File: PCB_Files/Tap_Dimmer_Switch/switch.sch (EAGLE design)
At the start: 37 parts, among them P1 HT7333

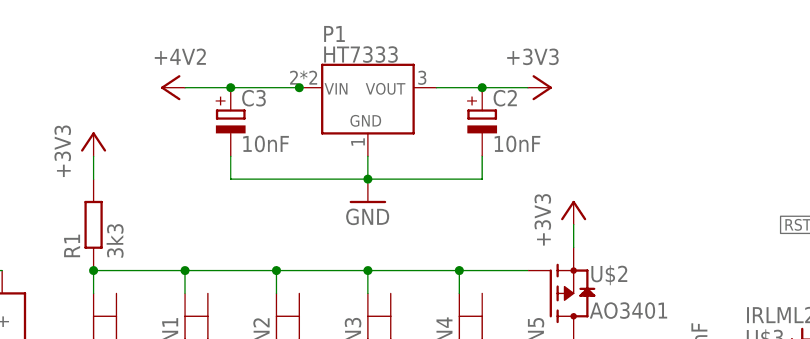
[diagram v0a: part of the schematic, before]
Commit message: created additional compact design of ws2812b module
this new design features smaller footprint, but the esp module ist partially outside the board, which will result in better wifi connection.

additionally the footprint of the HT7333 has been fixed as previously it had used the wrong package.
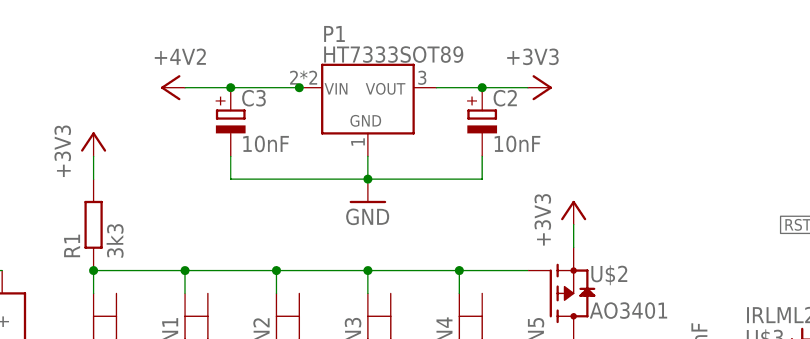
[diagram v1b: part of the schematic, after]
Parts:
- P1: value HT7333 -> HT7333SOT89; device diyHue:HT7333 -> diyHue:HT7333SOT89
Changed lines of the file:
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@@
 <part name="C1" library="rcl" deviceset="C-EU" device="025-025X050" value="10nF"/>
 <part name="GND9" library="supply1" deviceset="GND" device=""/>
-<part name="P1" library="diyHue" deviceset="HT7333" device=""/>
+<part name="P1" library="diyHue" deviceset="HT7333" device="SOT89"/>
 <part name="GND10" library="supply1" deviceset="GND" device=""/>
 <part name="FTDI" library="pinhead-2" deviceset="PINHD-1X06" device="_2.54-S"/>
